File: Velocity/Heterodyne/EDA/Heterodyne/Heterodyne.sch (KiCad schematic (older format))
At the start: 40 parts, among them J1 I2C, J3 PWR, J4 Doppler_Out, J5 V_Square, J7 Reciever, U1 SA612AD, U2 NE5532, U3 MAX7375AXR105, U4 MAX11613

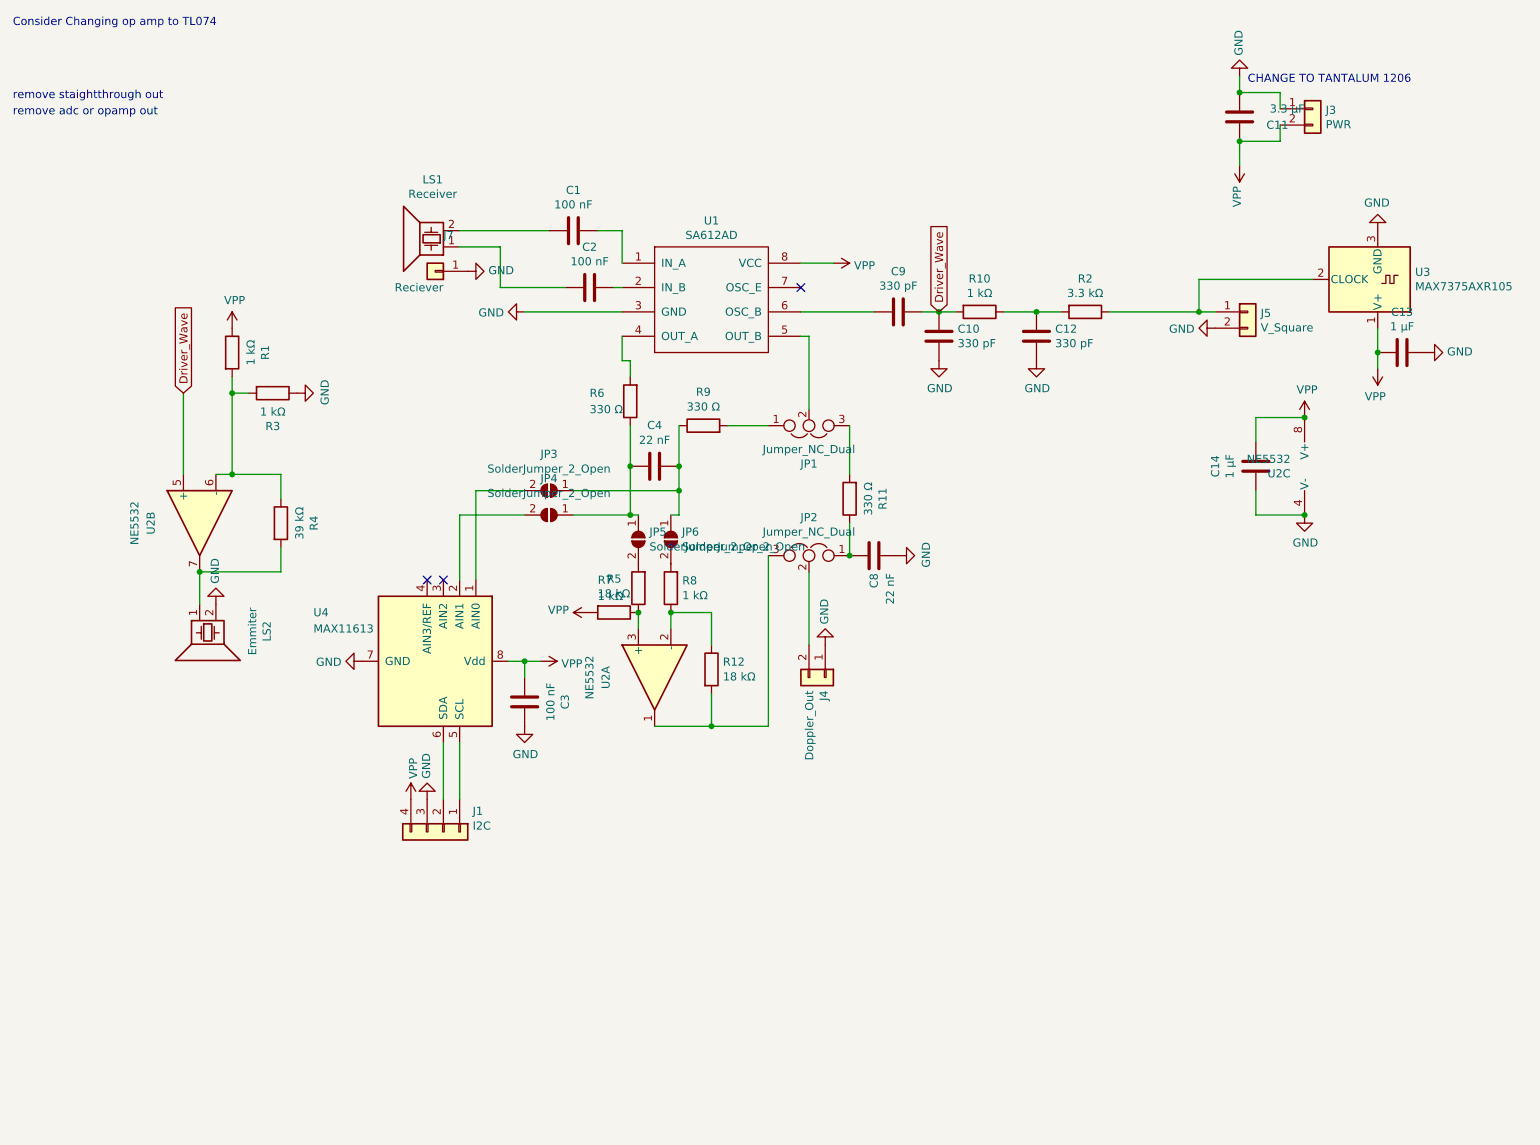
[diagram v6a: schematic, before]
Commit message: added  ATmega328P to velocity schematic
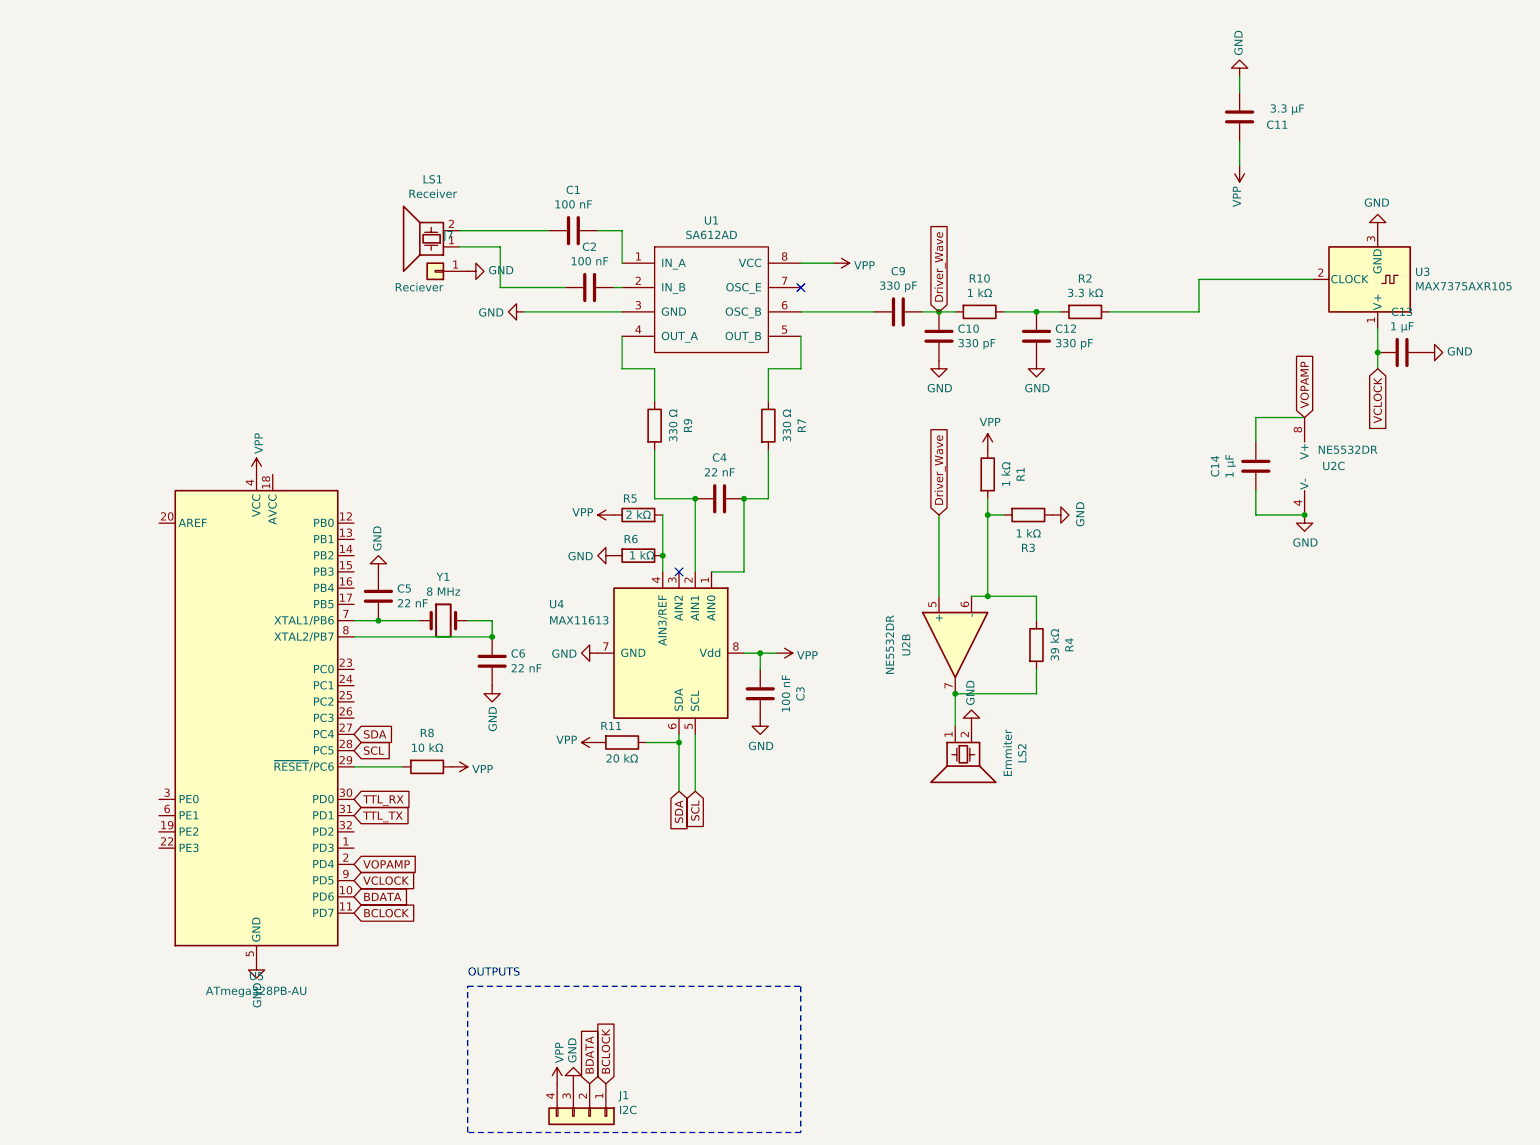
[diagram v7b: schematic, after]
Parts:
- removed C8: 22 nF, Capacitor_SMD:C_0805_2012Metric_Pad1.15x1.40mm_HandSolder, symbol Heterodyne-rescue:C-Device
- removed J3: PWR, Connector_PinHeader_2.54mm:PinHeader_1x02_P2.54mm_Vertical, symbol Heterodyne-rescue:Conn_01x02-Connector_Generic
- removed J4: Doppler_Out, Connector_PinHeader_2.54mm:PinHeader_1x02_P2.54mm_Vertical, symbol Heterodyne-rescue:Conn_01x02-Connector_Generic
- removed J5: V_Square, Connector_PinHeader_2.54mm:PinHeader_1x02_P2.54mm_Vertical, symbol Heterodyne-rescue:Conn_01x02-Connector_Generic
- removed JP1, JP2: Jumper_NC_Dual, Jumper:SolderJumper-3_P1.3mm_Open_Pad1.0x1.5mm, symbol Heterodyne-rescue:Jumper_NC_Dual-Device
- removed JP3, JP4, JP5, JP6: SolderJumper_2_Open, Jumper:SolderJumper-2_P1.3mm_Open_Pad1.0x1.5mm, symbol Jumper:SolderJumper_2_Open
- removed R11: 330 Ω, Resistor_SMD:R_0805_2012Metric_Pad1.15x1.40mm_HandSolder, symbol Heterodyne-rescue:R-Device
- removed R12: 18 kΩ, Resistor_SMD:R_0805_2012Metric_Pad1.15x1.40mm_HandSolder, symbol Device:R
- removed unit 1 of U2
- added C5, C6: 22 nF, Capacitor_SMD:C_0805_2012Metric, symbol Device:C
- added R11: 20 kΩ, Resistor_SMD:R_0805_2012Metric_Pad1.15x1.40mm_HandSolder, symbol Device:R
- added U5: ATmega328PB-AU, Package_QFP:TQFP-32_7x7mm_P0.8mm, symbol MCU_Microchip_ATmega:ATmega328PB-AU
- added Y1: 8 MHz, Crystal:Crystal_SMD_5032-2Pin_5.0x3.2mm, symbol Device:Crystal
- C11: footprint Capacitor_SMD:CP_Elec_8x10 -> Capacitor_SMD:C_1206_3216Metric_Pad1.42x1.75mm_HandSolder
- R5: value 18 kΩ -> 2 kΩ
- R6: value 330 Ω -> 1 kΩ
- R7: value 1 kΩ -> 330 Ω
- R8: value 1 kΩ -> 10 kΩ; footprint Resistor_SMD:R_0805_2012Metric_Pad1.15x1.40mm_HandSolder -> Resistor_SMD:R_0805_2012Metric
- U2: value NE5532 -> NE5532DR
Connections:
- net GND: now also R6.2, C5.1, C6.2, U5.21 (GND), U5.5 (GND)
- net VPP: now also R5.1, R8.1, R11.2, U5.4 (VCC); no longer C13.2, C14.1, R5.2, U2.8 (V+), U3.1 (V+)
- net at U1.4 (OUT_A): now also R9.1; no longer R6.2
- net at U1.5 (OUT_B): now also R7.1
- net at R9.2: now also C4.2, U4.2 (AIN1)
- net at R7.2: now also C4.1, U4.1 (AIN0)
- net at R8.2: now also U5.29 (~RESET~/PC6)
- net at R6.1: now also R5.2, U4.4 (AIN3/REF); no longer C4.2
- net BCLOCK: now reaches J1.1 (Pin_1)
- net BCLOCK: now also U5.11 (PD7); no longer U4.5 (SCL)
- net BDATA: now reaches J1.2 (Pin_2)
- net BDATA: now also U5.10 (PD6); no longer U4.6 (SDA)
- new net: C5.2, U5.7 (XTAL1/PB6), Y1.1
- new net: C6.1, U5.8 (XTAL2/PB7), Y1.2
- new net SCL: U4.5 (SCL), U5.28 (PC5)
- new net SDA: R11.1, U4.6 (SDA), U5.27 (PC4)
- new net TTL_RX: U5.30 (PD0)
- new net TTL_TX: U5.31 (PD1)
- new net VCLOCK: C13.2, U3.1 (V+), U5.9 (PD5)
- new net VOPAMP: C14.1, U2.8 (V+), U5.2 (PD4)
- no-connect marks 3 -> 2
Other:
- note added: "OUTPUTS"
- note removed: "CHANGE TO TANTALUM 1206"
- note removed: "Consider Changing op amp to TL074"
- note removed: "remove adc or opamp out\n"
- note removed: "remove staightthrough out"
- moved on the sheet: C3, C4, J1, LS2, R1, R3, R4, R9, U2B, U4

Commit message: added 4 layer PCB for heterodyne
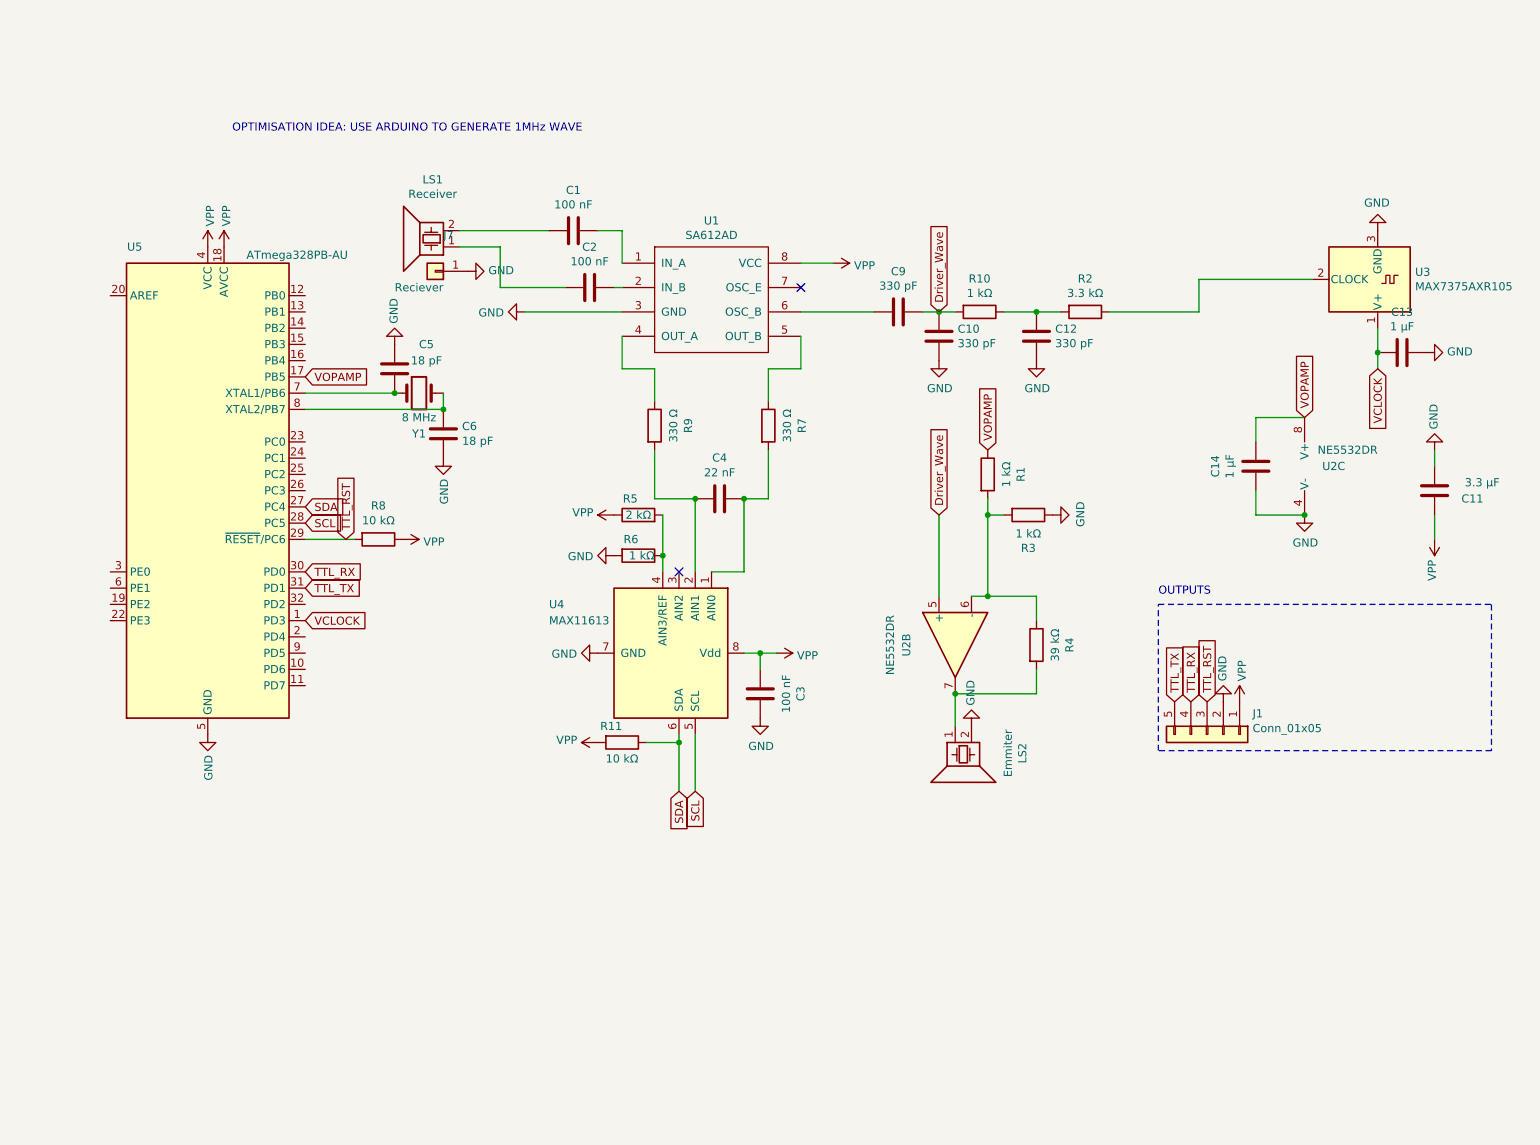
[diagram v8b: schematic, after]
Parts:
- removed J1: I2C, Connector_PinHeader_2.54mm:PinHeader_1x04_P2.54mm_Vertical, symbol Connector_Generic:Conn_01x04
- added J1: Conn_01x05, Connector_PinHeader_2.54mm:PinHeader_1x05_P2.54mm_Vertical, symbol Connector_Generic:Conn_01x05
- C1, C10, C12, C2, C3, C4, C9: footprint Capacitor_SMD:C_0805_2012Metric_Pad1.15x1.40mm_HandSolder -> Capacitor_SMD:C_0603_1608Metric_Pad1.05x0.95mm_HandSolder
- C11, C13, C14: footprint Capacitor_SMD:C_1206_3216Metric_Pad1.42x1.75mm_HandSolder -> Capacitor_SMD:C_0805_2012Metric
- C5, C6: value 22 nF -> 18 pF; footprint Capacitor_SMD:C_0805_2012Metric -> Capacitor_SMD:C_0603_1608Metric_Pad1.05x0.95mm_HandSolder
- R1, R10, R2, R3, R4, R5, R6, R7, R9: footprint Resistor_SMD:R_0805_2012Metric_Pad1.15x1.40mm_HandSolder -> Resistor_SMD:R_0603_1608Metric_Pad1.05x0.95mm_HandSolder
- R11: value 20 kΩ -> 10 kΩ; footprint Resistor_SMD:R_0805_2012Metric_Pad1.15x1.40mm_HandSolder -> Resistor_SMD:R_0603_1608Metric_Pad1.05x0.95mm_HandSolder
- R8: footprint Resistor_SMD:R_0805_2012Metric -> Resistor_SMD:R_0603_1608Metric_Pad1.05x0.95mm_HandSolder
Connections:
- net GND: now also J1.2 (Pin_2)
- net TTL_RX: now also J1.4 (Pin_4)
- net TTL_TX: now also J1.5 (Pin_5)
- net VCLOCK: now also U5.1 (PD3); no longer U5.9 (PD5)
- net VOPAMP: now also R1.1, U5.17 (PB5); no longer U5.2 (PD4)
- net VPP: now also U5.18 (AVCC), J1.1 (Pin_1); no longer R1.1
- net TTL_RST: now reaches R8.2, U5.29 (~RESET~/PC6)
- net TTL_RST: now also J1.3 (Pin_3)
- net BCLOCK: no longer names the net of U5.11 (PD7)
- net BDATA: no longer names the net of U5.10 (PD6)
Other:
- note added: "OPTIMISATION IDEA: USE ARDUINO TO GENERATE 1MHz WAVE"
- moved on the sheet: C11, C5, C6, R8, U5, Y1
